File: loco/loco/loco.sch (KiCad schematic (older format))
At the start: 21 parts, among them Q1 FDC6561AN, Q2 FDC6561AN, Q3 FDC6561AN, U1 STM32F030F4Px, U2 A4953_LJ, U3 TLV760

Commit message: Docs added
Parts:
- added C6: 2u2, Capacitor_SMD:C_0805_2012Metric, symbol Device:C
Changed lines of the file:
@@
 Wire Wire Line
 	3075 2875 3075 2600
+$Comp
+L Device:C C6
+U 1 1 5E67137D
+P 4625 2125
+F 0 "C6" H 4740 2171 50  0000 L CNN
+F 1 "2u2" H 4740 2080 50  0000 L CNN
+F 2 "Capacitor_SMD:C_0805_2012Metric" H 4663 1975 50  0001 C CNN
+F 3 "~" H 4625 2125 50  0001 C CNN
+	1    4625 2125
+	1    0    0    -1
+$EndComp
+$Comp
+L power:GND #PWR0116
+U 1 1 5E671387
+P 4625 2275
+F 0 "#PWR0116" H 4625 2025 50  0001 C CNN
+F 1 "GND" H 4630 2102 50  0001 C CNN
+F 2 "" H 4625 2275 50  0001 C CNN
+F 3 "" H 4625 2275 50  0001 C CNN
+	1    4625 2275
+	1    0    0    -1
+$EndComp
+Text Label 4625 1975 0    50   ~ 0
++3V3
 $EndSCHEMATC

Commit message: Routing done, mostly
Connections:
- wire segments 92 -> 94
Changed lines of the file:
@@
 	6550 4000 6550 4325
 Connection ~ 6550 4000
-Wire Wire Line
-	6550 4000 6750 4000
 Text Label 6550 4325 0    50   ~ 0
 SWDIO
@@
 	6325 4100 6325 4425
 Connection ~ 6325 4100
-Wire Wire Line
-	6325 4100 6750 4100
 Text Label 6325 4425 0    50   ~ 0
 SWCLK
@@
 Wire Wire Line
 	9275 3475 9725 3475
-Wire Wire Line
-	8675 3475 8400 3475
-Wire Wire Line
-	8675 3675 8400 3675
 $Comp
 L Device:R R6
@@
 Text Label 4625 1975 0    50   ~ 0
 +3V3
+Wire Wire Line
+	8200 4000 8200 3675
+Wire Wire Line
+	6550 4000 8200 4000
+Wire Wire Line
+	8200 3675 8675 3675
+Wire Wire Line
+	8000 4100 8000 3475
+Wire Wire Line
+	6325 4100 8000 4100
+Wire Wire Line
+	8000 3475 8675 3475
 $EndSCHEMATC

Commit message: Update
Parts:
- added C7: C, Capacitor_SMD:C_0603_1608Metric, symbol Device:C
- C6: value 2u2 -> 10u; footprint Capacitor_SMD:C_0805_2012Metric -> Capacitor_SMD:C_1206_3216Metric
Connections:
- net 27V: now also C7.1
- net GND: now also C7.2
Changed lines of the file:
@@
 P 4625 2125
 F 0 "C6" H 4740 2171 50  0000 L CNN
-F 1 "2u2" H 4740 2080 50  0000 L CNN
-F 2 "Capacitor_SMD:C_0805_2012Metric" H 4663 1975 50  0001 C CNN
+F 1 "10u" H 4740 2080 50  0000 L CNN
+F 2 "Capacitor_SMD:C_1206_3216Metric" H 4625 1825 50  0000 C CNN
 F 3 "~" H 4625 2125 50  0001 C CNN
 	1    4625 2125
@@
 Wire Wire Line
 	8000 3475 8675 3475
+$Comp
+L Device:C C7
+U 1 1 5E6743D7
+P 2175 2875
+F 0 "C7" H 2290 2921 50  0000 L CNN
+F 1 "C" H 2290 2830 50  0000 L CNN
+F 2 "Capacitor_SMD:C_0603_1608Metric" H 2213 2725 50  0001 C CNN
+F 3 "~" H 2175 2875 50  0001 C CNN
+	1    2175 2875
+	1    0    0    -1
+$EndComp
+$Comp
+L power:GND #PWR0117
+U 1 1 5E6743E1
+P 2175 3025
+F 0 "#PWR0117" H 2175 2775 50  0001 C CNN
+F 1 "GND" H 2180 2852 50  0001 C CNN
+F 2 "" H 2175 3025 50  0001 C CNN
+F 3 "" H 2175 3025 50  0001 C CNN
+	1    2175 3025
+	1    0    0    -1
+$EndComp
+Wire Wire Line
+	2175 2725 2175 2600
+Connection ~ 2175 2600
 $EndSCHEMATC

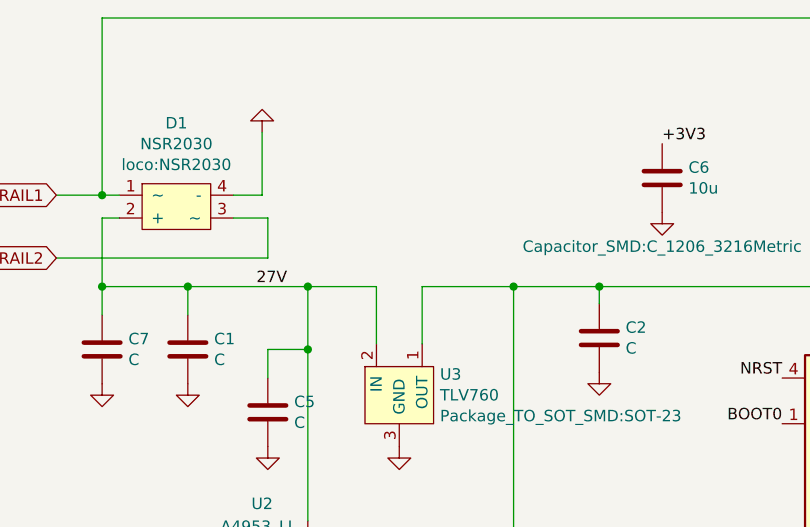
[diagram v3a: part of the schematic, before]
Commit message: LDO replacement
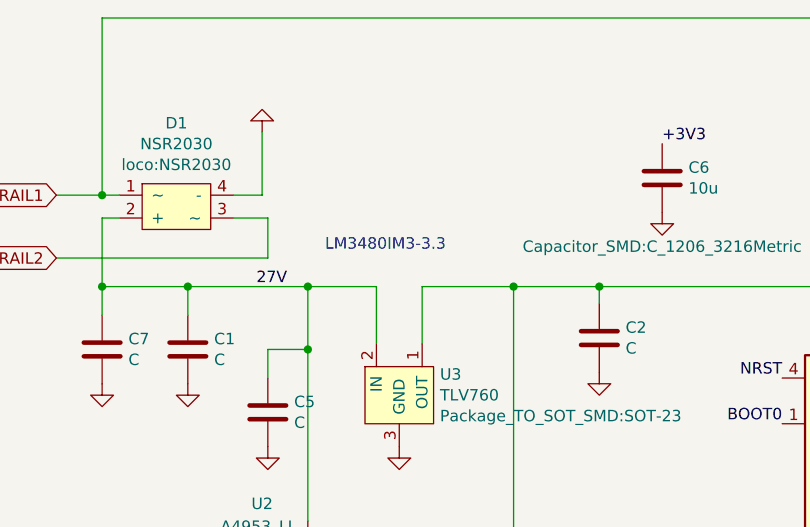
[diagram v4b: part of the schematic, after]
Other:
- note added: "LM3480IM3-3.3"
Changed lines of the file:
@@
 	2175 2725 2175 2600
 Connection ~ 2175 2600
+Text Notes 3150 2450 0    50   ~ 0
+LM3480IM3-3.3
 $EndSCHEMATC

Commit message: Values update
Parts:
- C1, C5, C7: value C -> 1uF 50V
- C2, C3: value C -> 1uF
- C6: value 10u -> 10uF
- R1: value TBD -> 22K
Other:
- moved on the sheet: C2, C3, C5, C6, D1, R1, R2, R3

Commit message: Update loco.sch
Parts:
- R1: value 22K -> 33K
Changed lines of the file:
@@
 P 7500 2075
 F 0 "R1" H 7570 2121 50  0000 L CNN
-F 1 "22K" H 7570 2030 50  0000 L CNN
+F 1 "33K" H 7570 2030 50  0000 L CNN
 F 2 "Resistor_SMD:R_0603_1608Metric" V 7430 2075 50  0001 C CNN
 F 3 "~" H 7500 2075 50  0001 C CNN
